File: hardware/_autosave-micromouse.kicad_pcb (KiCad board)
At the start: 2 copper layers, 105 x 74 mm, 77 parts, among them CN1 5_PIN_HEADER, CN2 5_PIN_HEADER, J1 uSD_SLOT_47219-2001, M1 MOTOR_MOUNTS_AND_ENCODERS, M3 2.54MM-SLIDE-SWITCH_TS02_SWIT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, SW1 SWITCH_DPST, SW2 SWITCH_DPST, SW3 SWITCH_DPST, U1 STM32F446RE_LQFP64, U10 MPU-9250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

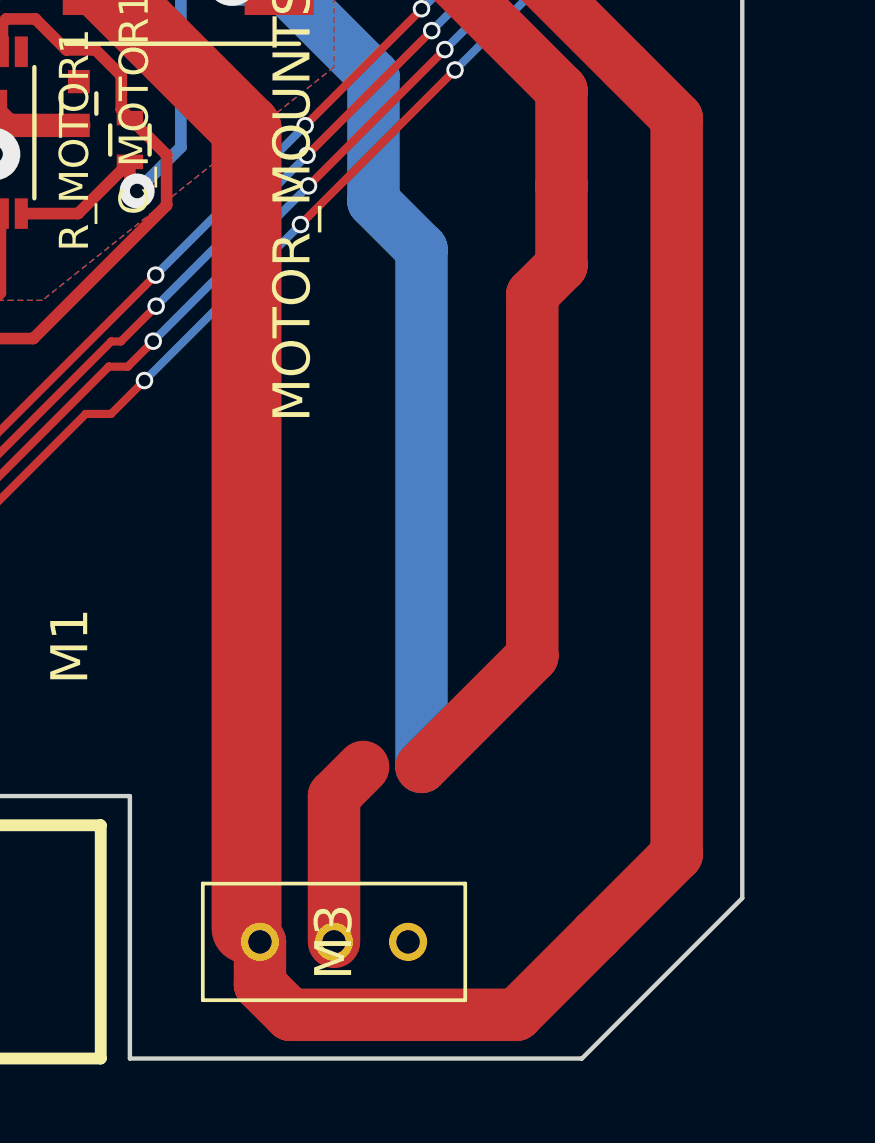
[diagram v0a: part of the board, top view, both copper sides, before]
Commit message: PCB board- needs to check the motor driver
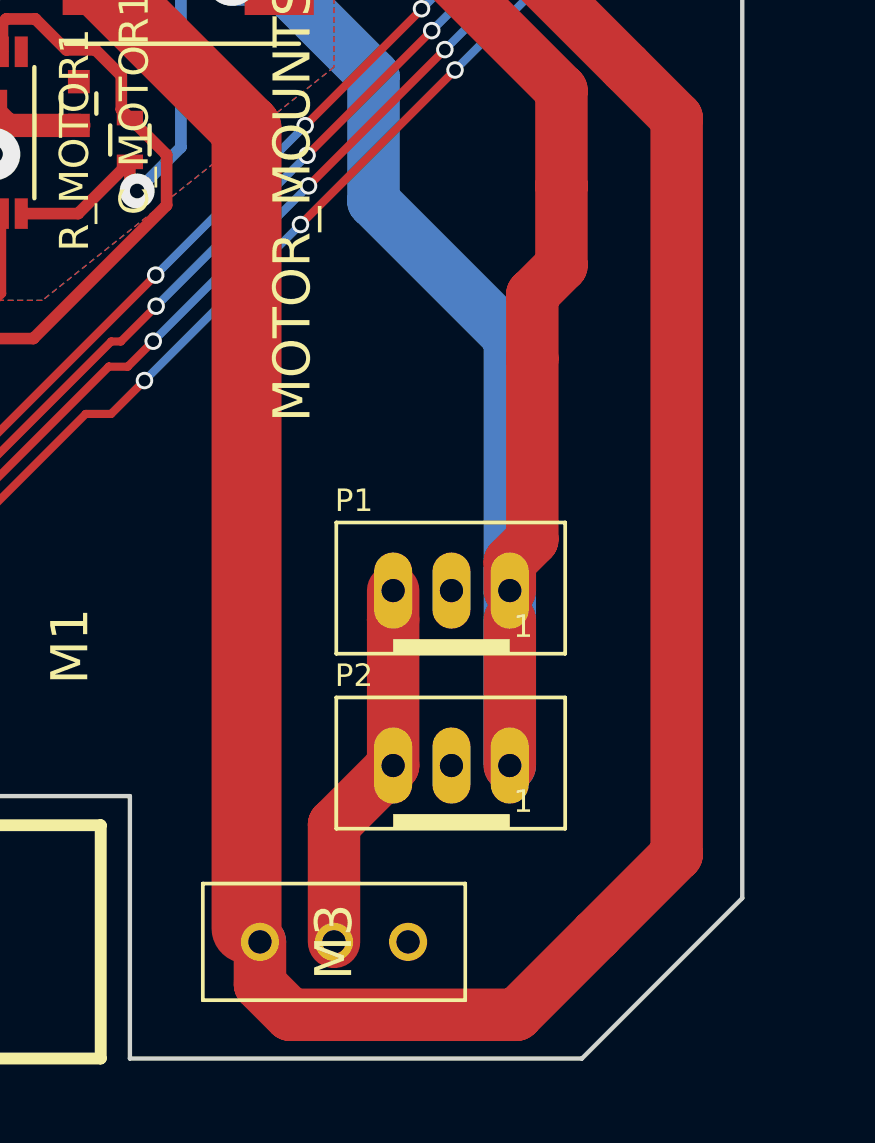
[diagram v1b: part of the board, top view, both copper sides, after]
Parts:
- added P1: B3B-PH-SM4-TB, footprints_micromouse:JST_B3B-PH_HEADER, F.Cu at (229.0, 111.0)
- added P2: B3B-PH-SM4-TB, footprints_micromouse:JST_B3B-PH_HEADER, F.Cu at (229.0, 117.0)
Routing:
- net Net-(M3-PadPIN2): track 6.41 -> 12.9 mm
- net GND: track 487.0 -> 485.9 mm
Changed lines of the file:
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@@
 (kicad_pcb (version 4) (host pcbnew 4.0.2-stable)
   (general
-    (links 251)
-    (no_connects 7)
+    (links 255)
+    (no_connects 6)
     (area 133.924999 52.924999 239.075001 127.075001)
     (thickness 1.6)
     (drawings 34)
-    (tracks 1227)
+    (tracks 1233)
     (zones 0)
-    (modules 77)
-    (nets 112)
+    (modules 79)
+    (nets 114)
   )
   (page A4)
@@
   (net 110 LED2)
   (net 111 "Net-(M3-PadPIN2)")
+  (net 112 "Net-(P1-Pad2)")
+  (net 113 "Net-(P2-Pad2)")
   (net_class Default "This is the default net class."
     (clearance 0.15)
@@
     (add_net "Net-(M3-PadPIN1)")
     (add_net "Net-(M3-PadPIN2)")
+    (add_net "Net-(P1-Pad2)")
+    (add_net "Net-(P2-Pad2)")
     (add_net "Net-(R13-Pad1)")
     (add_net "Net-(R14-Pad1)")
@@
     )
   )
+  (module footprints_micromouse:JST_B3B-PH_HEADER (layer F.Cu)
+    (at 229 111)
+    (descr "3-pin JST PH Shrouded Header <br>\n2.0mm pitch <br>\nP/N B3B-PH-K-S.  Mating plug PHR-3 <br>")
+    (fp_text reference P1 (at -3.9725 -2.6825) (layer F.SilkS)
+      (effects (font (size 0.77216 0.77216) (thickness 0.065024)) (justify left bottom))
+    )
+    (fp_text value B3B-PH-SM4-TB (at -1 4) (layer F.SilkS) hide
+      (effects (font (thickness 0.15)))
+    )
+    (fp_line (start -3.9225 -2.3825) (end 3.9275 -2.3825) (layer F.SilkS) (width 0.127))
+    (fp_line (start 3.9275 -2.3825) (end 3.9275 2.1175) (layer F.SilkS) (width 0.127))
+    (fp_line (start 3.9275 2.1175) (end -3.9225 2.1175) (layer F.SilkS) (width 0.127))
+    (fp_line (start -3.9225 2.1175) (end -3.9225 -2.3825) (layer F.SilkS) (width 0.127))
+    (fp_poly (pts (xy -1.9725 2.1175) (xy 2.0275 2.1175) (xy 2.0275 1.6175) (xy -1.9725 1.6175)) (layer F.SilkS) (width 0))
+    (fp_text user 1 (at 2.145 1.635) (layer F.SilkS)
+      (effects (font (size 0.77216 0.77216) (thickness 0.065024)) (justify left bottom))
+    )
+    (pad 3 thru_hole oval (at -1.9725 -0.0475 90) (size 2.616 1.308) (drill 0.8) (layers *.Cu *.Mask)
+      (net 111 "Net-(M3-PadPIN2)"))
+    (pad 2 thru_hole oval (at 0.0275 -0.0475 90) (size 2.616 1.308) (drill 0.8) (layers *.Cu *.Mask)
+      (net 112 "Net-(P1-Pad2)"))
+    (pad 1 thru_hole oval (at 2.0275 -0.0475 90) (size 2.616 1.308) (drill 0.8) (layers *.Cu *.Mask)
+      (net 1 GND))
+  )
+  (module footprints_micromouse:JST_B3B-PH_HEADER (layer F.Cu)
+    (at 229 117)
+    (descr "3-pin JST PH Shrouded Header <br>\n2.0mm pitch <br>\nP/N B3B-PH-K-S.  Mating plug PHR-3 <br>")
+    (fp_text reference P2 (at -3.9725 -2.6825) (layer F.SilkS)
+      (effects (font (size 0.77216 0.77216) (thickness 0.065024)) (justify left bottom))
+    )
+    (fp_text value B3B-PH-SM4-TB (at -1 4) (layer F.SilkS) hide
+      (effects (font (thickness 0.15)))
+    )
+    (fp_line (start -3.9225 -2.3825) (end 3.9275 -2.3825) (layer F.SilkS) (width 0.127))
+    (fp_line (start 3.9275 -2.3825) (end 3.9275 2.1175) (layer F.SilkS) (width 0.127))
+    (fp_line (start 3.9275 2.1175) (end -3.9225 2.1175) (layer F.SilkS) (width 0.127))
+    (fp_line (start -3.9225 2.1175) (end -3.9225 -2.3825) (layer F.SilkS) (width 0.127))
+    (fp_poly (pts (xy -1.9725 2.1175) (xy 2.0275 2.1175) (xy 2.0275 1.6175) (xy -1.9725 1.6175)) (layer F.SilkS) (width 0))
+    (fp_text user 1 (at 2.145 1.635) (layer F.SilkS)
+      (effects (font (size 0.77216 0.77216) (thickness 0.065024)) (justify left bottom))
+    )
+    (pad 3 thru_hole oval (at -1.9725 -0.0475 90) (size 2.616 1.308) (drill 0.8) (layers *.Cu *.Mask)
+      (net 111 "Net-(M3-PadPIN2)"))
+    (pad 2 thru_hole oval (at 0.0275 -0.0475 90) (size 2.616 1.308) (drill 0.8) (layers *.Cu *.Mask)
+      (net 113 "Net-(P2-Pad2)"))
+    (pad 1 thru_hole oval (at 2.0275 -0.0475 90) (size 2.616 1.308) (drill 0.8) (layers *.Cu *.Mask)
+      (net 1 GND))
+  )
   (gr_line (start 218 53) (end 232.5 53) (angle 90) (layer Edge.Cuts) (width 0.15))
   (gr_line (start 218 127) (end 233.5 127) (angle 90) (layer Edge.Cuts) (width 0.15))
@@
   (segment (start 180 91.5) (end 179.5 91.5) (width 0.8) (layer B.Cu) (net 0))
   (segment (start 179.5 91.5) (end 176.5 88.5) (width 0.8) (layer B.Cu) (net 0))
-  (segment (start 228 117) (end 228 99.25) (width 1.8) (layer B.Cu) (net 1))
-  (via (at 221.5 90) (size 1.8) (drill 0.6) (layers F.Cu B.Cu) (net 1))
+  (segment (start 231.0275 110.9525) (end 231.0275 116.9525) (width 1.8) (layer B.Cu) (net 1))
+  (segment (start 231.0275 110.9525) (end 231.0275 109.9725) (width 1.8) (layer F.Cu) (net 1))
+  (segment (start 231.0275 109.9725) (end 231.8 109.2) (width 1.8) (layer F.Cu) (net 1))
+  (segment (start 231.0275 110.9525) (end 231.0275 102.2775) (width 1.8) (layer B.Cu) (net 1))
   (segment (start 221.5 90) (end 223.12 90) (width 1.5) (layer F.Cu) (net 1))
   (segment (start 223.05 90) (end 221.5 90) (width 1.8) (layer B.Cu) (net 1))
   (segment (start 226.35 93.3) (end 223.05 90) (width 1.8) (layer B.Cu) (net 1))
   (segment (start 226.35 97.6) (end 226.35 93.3) (width 1.8) (layer B.Cu) (net 1))
-  (segment (start 228 99.25) (end 226.35 97.6) (width 1.8) (layer B.Cu) (net 1))
+  (via (at 221.5 90) (size 1.8) (drill 0.6) (layers F.Cu B.Cu) (net 1))
+  (segment (start 231.0275 102.2775) (end 226.35 97.6) (width 1.8) (layer B.Cu) (net 1))
+  (segment (start 231.0275 116.9525) (end 231.0275 111.9525) (width 1.8) (layer F.Cu) (net 1))
+  (segment (start 231.8 103) (end 231.8 109.2) (width 1.8) (layer F.Cu) (net 1))
   (segment (start 173.025 108.5) (end 173.3 108.5) (width 0.8) (layer F.Cu) (net 1))
   (segment (start 173.3 108.5) (end 174.6 109.8) (width 0.8) (layer F.Cu) (net 1))
@@
   (segment (start 182.8 72.4) (end 182.8 72.4) (width 0.8) (layer F.Cu) (net 1))
   (segment (start 186.8 72.2) (end 186.6 72.4) (width 1.5) (layer F.Cu) (net 1))
-  (segment (start 228 117) (end 231.8 113.2) (width 1.8) (layer F.Cu) (net 1))
   (segment (start 186.8 72.2) (end 194 72.2) (width 1.8) (layer F.Cu) (net 1))
   (segment (start 194 72.2) (end 211.2 72.2) (width 1.8) (layer F.Cu) (net 1))
@@
   (segment (start 232.8 97.075) (end 232.8 99.8) (width 1.8) (layer F.Cu) (net 1))
   (segment (start 231.8 100.8) (end 232.8 99.8) (width 1.8) (layer F.Cu) (net 1))
-  (segment (start 231.8 113.2) (end 231.8 100.8) (width 1.8) (layer F.Cu) (net 1))
+  (segment (start 231.8 103) (end 231.8 100.8) (width 1.8) (layer F.Cu) (net 1))
   (segment (start 176.249937 95.749938) (end 176.249937 94.820063) (width 0.28) (layer F.Cu) (net 4))
   (segment (start 183.53 109.85) (end 169.38 124) (width 0.28) (layer B.Cu) (net 4))
@@
   (via (at 180.8 93.6) (size 0.6) (drill 0.4) (layers F.Cu B.Cu) (net 110))
   (segment (start 180.749938 93.650062) (end 180.8 93.6) (width 0.28) (layer F.Cu) (net 110))
-  (segment (start 226 117) (end 225 118) (width 1.8) (layer F.Cu) (net 111))
-  (segment (start 225 118) (end 225 123) (width 1.8) (layer F.Cu) (net 111))
+  (segment (start 227.0275 110.9525) (end 227.0275 111.9525) (width 1.8) (layer F.Cu) (net 111))
+  (segment (start 227.0275 116.9525) (end 227.0275 111.9525) (width 1.8) (layer F.Cu) (net 111))
+  (segment (start 225 123) (end 225 118.98) (width 1.8) (layer F.Cu) (net 111))
+  (segment (start 225 118.98) (end 227.0275 116.9525) (width 1.8) (layer F.Cu) (net 111))
   (zone (net 13) (net_name +BATT) (layer F.Cu) (hatch edge 0.508)
     (connect_pads (clearance 0.05))
